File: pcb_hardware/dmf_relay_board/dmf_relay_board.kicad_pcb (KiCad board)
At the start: 2 copper layers, 100 x 96.5 mm, 64 parts, among them J1 HVPS, J2 Relays to Electrodes 1, J3 Relays to Electrodes 2, J4 Electrodes from Relay 1, J5 Electrodes from Relay 2, U1 HV507

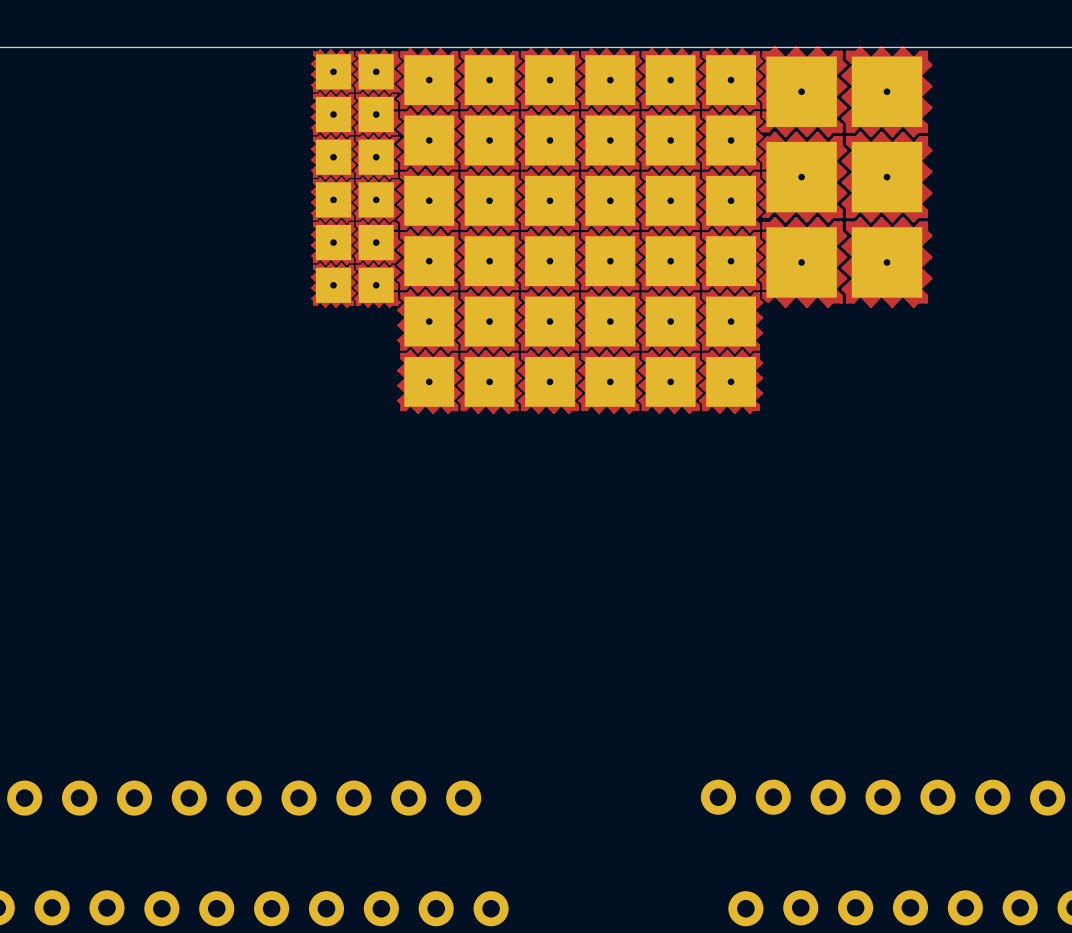
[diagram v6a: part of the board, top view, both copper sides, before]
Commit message: electrode footprints placed - routing now
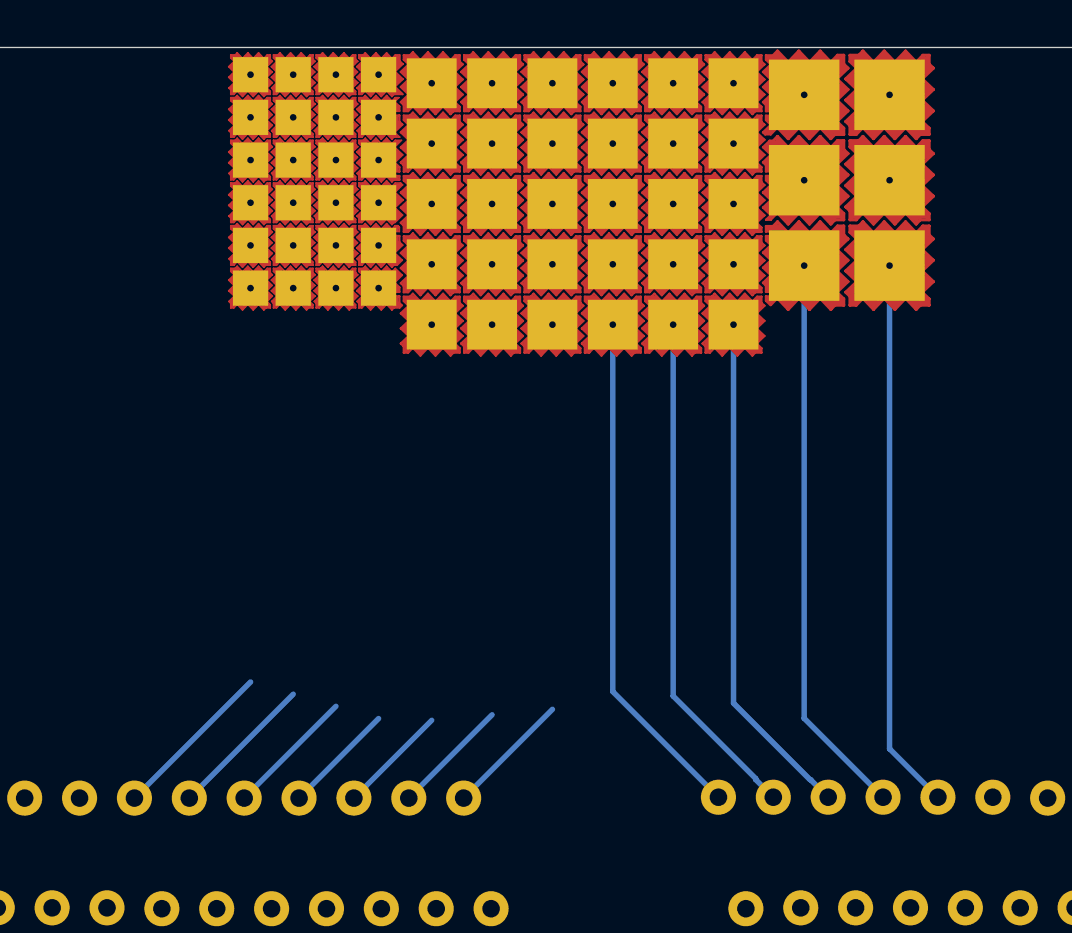
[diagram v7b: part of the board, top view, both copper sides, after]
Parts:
- removed E1, E10, E11, E12, E13, E14, E15, E16, E17, E18, E19, E2, E20, E21, E22, E23, E24, E25, E26, E27, E28, E29, E3, E30, E31, E32, E33, E34, E35, E36, E4, E5, E6, E7, E8, E9: ELEC_SML, dmf_relay_board:ELECTRODE_2_75_4MIL_4_5
- removed E50, E51, E52, E53, E54, E55: ELEC_XS, dmf_relay_board:ELECTRODE_1_375_4MIL_4_5
- removed the REF** at (174.5, 63.8)
- removed the REF** at (151.2, 61.0)
- removed the REF** at (151.2, 59.0)
- removed the REF** at (151.2, 57.1)
- removed the REF** at (151.2, 55.2)
- removed the REF** at (174.5, 59.9)
- removed the REF** at (174.5, 56.1)
- removed the REF** at (170.6, 63.8)
- removed the REF** at (170.6, 59.9)
- removed the REF** at (170.6, 56.1)
- removed the REF** at (151.2, 64.9)
- removed the REF** at (151.2, 62.9)
- added ELG1: ELEC_SM_TO_LG_1, dmf_relay_board:ELEC_SM_TO_LG_NUM1, F.Cu at (170.7, 56.2)
- added ELG2: ELEC_LG, dmf_relay_board:ELECTRODE_3_89_4MIL_4_5, F.Cu at (174.6, 56.2)
- added ELG3: ELEC_SM_TO_LG_2, dmf_relay_board:ELEC_SM_TO_LG_NUM2, F.Cu at (170.7, 60.1)
- added ELG4: ELEC_LG, dmf_relay_board:ELECTRODE_3_89_4MIL_4_5, F.Cu at (174.6, 60.1)
- added ELG5: ELEC_SM_TO_LG_3, dmf_relay_board:ELEC_SM_TO_LG_NUM3, F.Cu at (170.7, 64.0)
- added ELG6: ELEC_LG, dmf_relay_board:ELECTRODE_3_89_4MIL_4_5, F.Cu at (174.6, 64.0)
- added ESM1: ELEC_SML, dmf_relay_board:ELECTRODE_2_75_4MIL_4_5, F.Cu at (153.7, 55.7)
- added ESM10: ELEC_SML, dmf_relay_board:ELECTRODE_2_75_4MIL_4_5, F.Cu at (162.0, 58.4)
- added ESM11: ELEC_SML, dmf_relay_board:ELECTRODE_2_75_4MIL_4_5, F.Cu at (164.7, 58.4)
- added ESM12: ELEC_SML, dmf_relay_board:ELECTRODE_2_75_4MIL_4_5, F.Cu at (167.5, 58.4)
- added ESM13: ELEC_SML, dmf_relay_board:ELECTRODE_2_75_4MIL_4_5, F.Cu at (153.7, 61.2)
- added ESM14: ELEC_SML, dmf_relay_board:ELECTRODE_2_75_4MIL_4_5, F.Cu at (156.5, 61.2)
- added ESM15: ELEC_SML, dmf_relay_board:ELECTRODE_2_75_4MIL_4_5, F.Cu at (159.2, 61.2)
- added ESM16: ELEC_SML, dmf_relay_board:ELECTRODE_2_75_4MIL_4_5, F.Cu at (162.0, 61.2)
- added ESM17: ELEC_SML, dmf_relay_board:ELECTRODE_2_75_4MIL_4_5, F.Cu at (164.7, 61.2)
- added ESM18: ELEC_SML, dmf_relay_board:ELECTRODE_2_75_4MIL_4_5, F.Cu at (167.5, 61.2)
- added ESM19: ELEC_SML, dmf_relay_board:ELECTRODE_2_75_4MIL_4_5, F.Cu at (153.7, 63.9)
- added ESM2: ELEC_SML, dmf_relay_board:ELECTRODE_2_75_4MIL_4_5, F.Cu at (156.5, 55.7)
- added ESM20: ELEC_SML, dmf_relay_board:ELECTRODE_2_75_4MIL_4_5, F.Cu at (156.5, 63.9)
- added ESM21: ELEC_SML, dmf_relay_board:ELECTRODE_2_75_4MIL_4_5, F.Cu at (159.2, 63.9)
- added ESM22: ELEC_SML, dmf_relay_board:ELECTRODE_2_75_4MIL_4_5, F.Cu at (162.0, 63.9)
- added ESM23: ELEC_SML, dmf_relay_board:ELECTRODE_2_75_4MIL_4_5, F.Cu at (164.7, 63.9)
- added ESM24: ELEC_SML, dmf_relay_board:ELECTRODE_2_75_4MIL_4_5, F.Cu at (167.5, 63.9)
- added ESM25: ELEC_SML, dmf_relay_board:ELECTRODE_2_75_4MIL_4_5, F.Cu at (153.7, 66.7)
- added ESM26: ELEC_SML, dmf_relay_board:ELECTRODE_2_75_4MIL_4_5, F.Cu at (156.5, 66.7)
- added ESM27: ELEC_SML, dmf_relay_board:ELECTRODE_2_75_4MIL_4_5, F.Cu at (159.2, 66.7)
- added ESM28: ELEC_SML, dmf_relay_board:ELECTRODE_2_75_4MIL_4_5, F.Cu at (162.0, 66.7)
- added ESM29: ELEC_SML, dmf_relay_board:ELECTRODE_2_75_4MIL_4_5, F.Cu at (164.7, 66.7)
- added ESM3: ELEC_SML, dmf_relay_board:ELECTRODE_2_75_4MIL_4_5, F.Cu at (159.2, 55.7)
- added ESM30: ELEC_SML, dmf_relay_board:ELECTRODE_2_75_4MIL_4_5, F.Cu at (167.5, 66.7)
- added ESM4: ELEC_SML, dmf_relay_board:ELECTRODE_2_75_4MIL_4_5, F.Cu at (162.0, 55.7)
- added ESM5: ELEC_SML, dmf_relay_board:ELECTRODE_2_75_4MIL_4_5, F.Cu at (164.7, 55.7)
- added ESM6: ELEC_SML, dmf_relay_board:ELECTRODE_2_75_4MIL_4_5, F.Cu at (167.5, 55.7)
- added ESM7: ELEC_SML, dmf_relay_board:ELECTRODE_2_75_4MIL_4_5, F.Cu at (153.7, 58.4)
- added ESM8: ELEC_SML, dmf_relay_board:ELECTRODE_2_75_4MIL_4_5, F.Cu at (156.5, 58.4)
- added ESM9: ELEC_SML, dmf_relay_board:ELECTRODE_2_75_4MIL_4_5, F.Cu at (159.2, 58.4)
- added EXS1: ELEC_XS, dmf_relay_board:ELECTRODE_1_375_4MIL_4_5, F.Cu at (145.5, 55.3)
- added EXS10: ELEC_XS, dmf_relay_board:ELECTRODE_1_375_4MIL_4_5, F.Cu at (147.4, 59.2)
- added EXS11: ELEC_XS, dmf_relay_board:ELECTRODE_1_375_4MIL_4_5, F.Cu at (149.4, 59.2)
- added EXS12: ELEC_XS_TO_SM_3, dmf_relay_board:ELEC_XS_TO_SM_NUM3, F.Cu at (151.3, 59.2)
- added EXS13: ELEC_XS, dmf_relay_board:ELECTRODE_1_375_4MIL_4_5, F.Cu at (145.5, 61.1)
- added EXS14: ELEC_XS, dmf_relay_board:ELECTRODE_1_375_4MIL_4_5, F.Cu at (147.4, 61.1)
- added EXS15: ELEC_XS, dmf_relay_board:ELECTRODE_1_375_4MIL_4_5, F.Cu at (149.4, 61.1)
- added EXS16: ELEC_XS_TO_SM_4, dmf_relay_board:ELEC_XS_TO_SM_NUM4, F.Cu at (151.3, 61.1)
- added EXS17: ELEC_XS, dmf_relay_board:ELECTRODE_1_375_4MIL_4_5, F.Cu at (145.5, 63.1)
- added EXS18: ELEC_XS, dmf_relay_board:ELECTRODE_1_375_4MIL_4_5, F.Cu at (147.4, 63.1)
- added EXS19: ELEC_XS, dmf_relay_board:ELECTRODE_1_375_4MIL_4_5, F.Cu at (149.4, 63.1)
- added EXS2: ELEC_XS, dmf_relay_board:ELECTRODE_1_375_4MIL_4_5, F.Cu at (147.4, 55.3)
- added EXS20: ELEC_XS_TO_SM_5, dmf_relay_board:ELEC_XS_TO_SM_NUM5, F.Cu at (151.3, 63.1)
- added EXS21: ELEC_XS, dmf_relay_board:ELECTRODE_1_375_4MIL_4_5, F.Cu at (145.5, 65.0)
- added EXS22: ELEC_XS, dmf_relay_board:ELECTRODE_1_375_4MIL_4_5, F.Cu at (147.4, 65.0)
- added EXS23: ELEC_XS, dmf_relay_board:ELECTRODE_1_375_4MIL_4_5, F.Cu at (149.4, 65.0)
- added EXS24: ELEC_XS_TO_SM_6, dmf_relay_board:ELEC_XS_TO_SM_NUM6, F.Cu at (151.3, 65.0)
- added EXS3: ELEC_XS, dmf_relay_board:ELECTRODE_1_375_4MIL_4_5, F.Cu at (149.4, 55.3)
- added EXS4: ELEC_XS_TO_SM_1, dmf_relay_board:ELEC_XS_TO_SM_NUM1, F.Cu at (151.3, 55.3)
- added EXS5: ELEC_XS, dmf_relay_board:ELECTRODE_1_375_4MIL_4_5, F.Cu at (145.5, 57.2)
- added EXS6: ELEC_XS, dmf_relay_board:ELECTRODE_1_375_4MIL_4_5, F.Cu at (147.4, 57.2)
- added EXS7: ELEC_XS, dmf_relay_board:ELECTRODE_1_375_4MIL_4_5, F.Cu at (149.4, 57.2)
- added EXS8: ELEC_XS_TO_SM_2, dmf_relay_board:ELEC_XS_TO_SM_NUM2, F.Cu at (151.3, 57.2)
- added EXS9: ELEC_XS, dmf_relay_board:ELECTRODE_1_375_4MIL_4_5, F.Cu at (145.5, 59.2)
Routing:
- net Net-(ELG5-Pad1): track 0.00 -> 25.7 mm
- net Net-(ELG6-Pad1): track 0.00 -> 25.1 mm
- net Net-(ESM28-Pad1): track 0.00 -> 23.5 mm
- net Net-(ESM29-Pad1): track 0.00 -> 23.4 mm
- net Net-(ESM30-Pad1): track 0.00 -> 23.3 mm
- net Net-(EXS21-Pad1): track 0.00 -> 7.48 mm
- net Net-(EXS22-Pad1): track 0.00 -> 6.70 mm
- net Net-(EXS23-Pad1): track 0.00 -> 5.91 mm
- net Net-(ESM27-Pad1): track 0.00 -> 5.72 mm
- net Net-(ESM26-Pad1): track 0.00 -> 5.37 mm
- net Net-(EXS24-Pad1): track 0.00 -> 5.13 mm
- net Net-(ESM25-Pad1): track 0.00 -> 5.01 mm

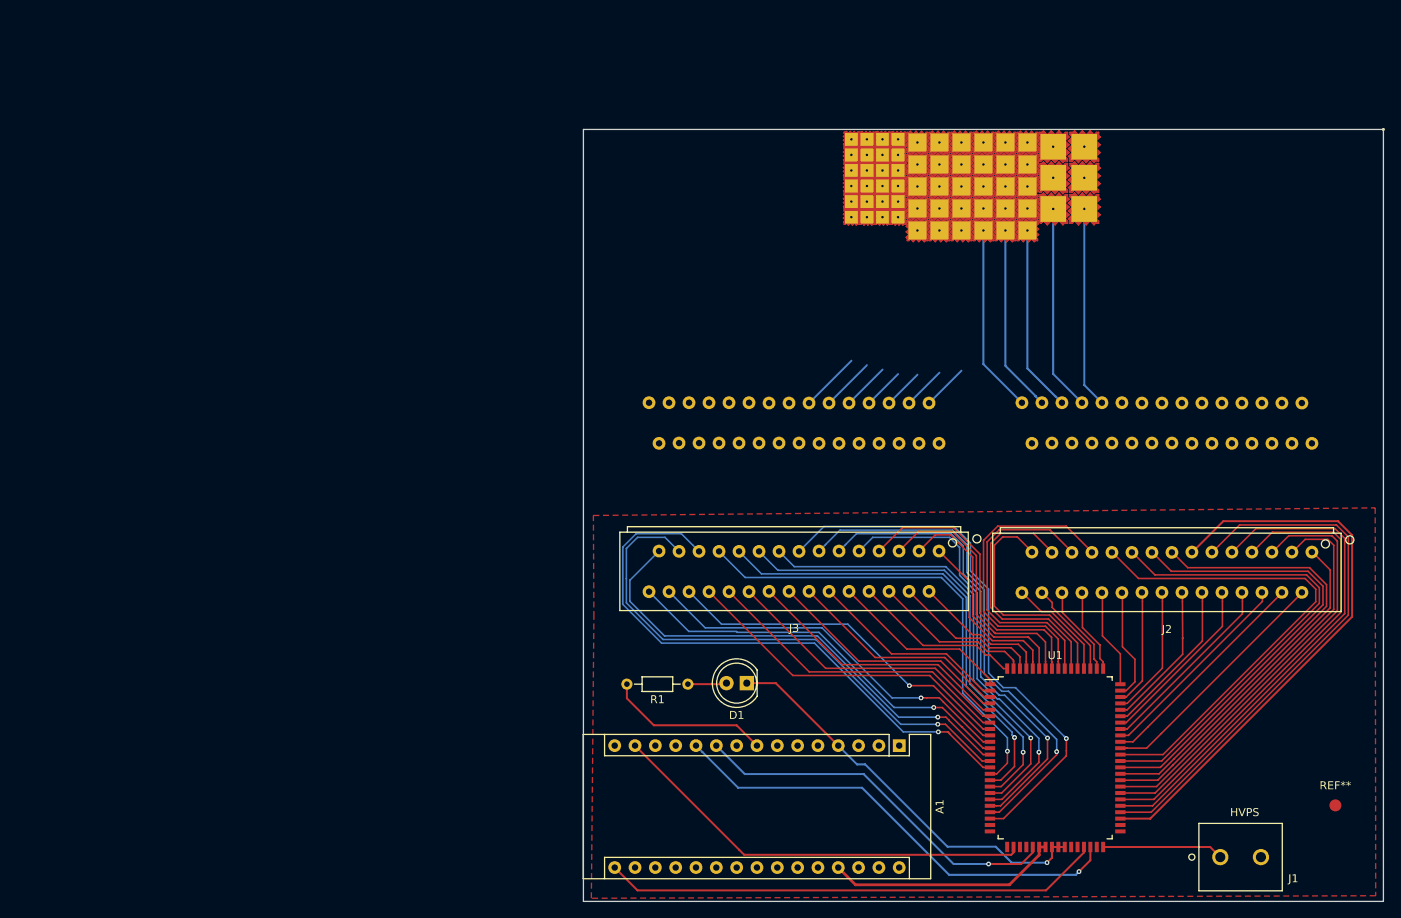
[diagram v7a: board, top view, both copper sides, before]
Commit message: electrode pads fixed for routing
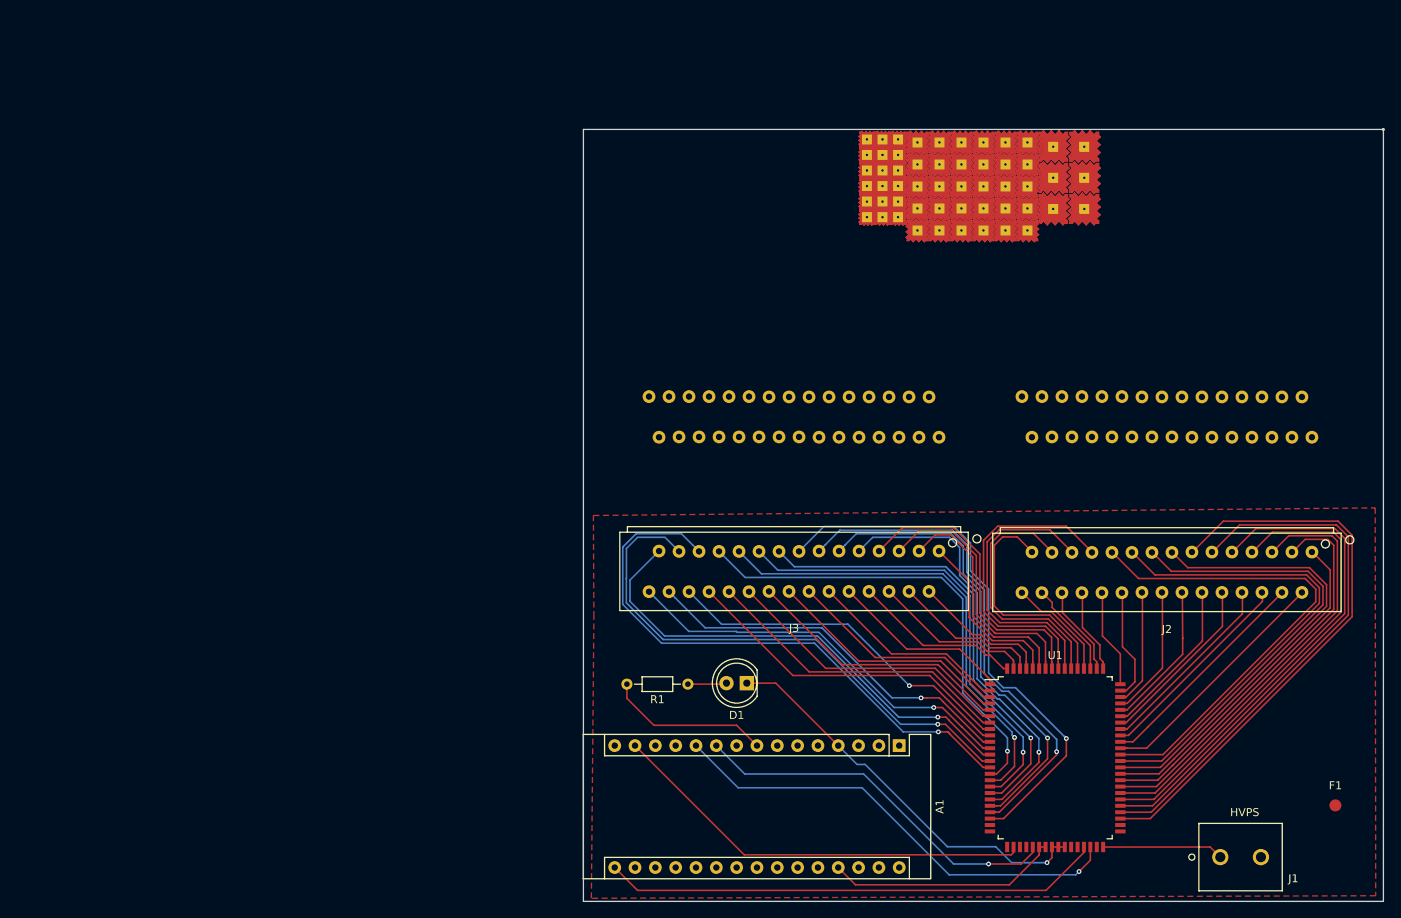
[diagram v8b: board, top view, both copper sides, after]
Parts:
- removed EXS19, EXS21, EXS22, EXS23: ELEC_XS, dmf_relay_board:ELECTRODE_1_375_4MIL_4_5
- removed EXS20: ELEC_XS_TO_SM_5, dmf_relay_board:ELEC_XS_TO_SM_NUM5
- removed EXS24: ELEC_XS_TO_SM_6, dmf_relay_board:ELEC_XS_TO_SM_NUM6
- EXS12: value ELEC_XS_TO_SM_3 -> ELEC_XS_TO_SM_4; footprint dmf_relay_board:ELEC_XS_TO_SM_NUM3 -> dmf_relay_board:ELEC_XS_TO_SM_NUM4
- EXS15: value ELEC_XS -> ELEC_XS_TO_SM_5; footprint dmf_relay_board:ELECTRODE_1_375_4MIL_4_5 -> dmf_relay_board:ELEC_XS_TO_SM_NUM5
- EXS16: value ELEC_XS_TO_SM_4 -> ELEC_XS; footprint dmf_relay_board:ELEC_XS_TO_SM_NUM4 -> dmf_relay_board:ELECTRODE_1_375_4MIL_4_5
- EXS18: value ELEC_XS -> ELEC_XS_TO_SM_6; footprint dmf_relay_board:ELECTRODE_1_375_4MIL_4_5 -> dmf_relay_board:ELEC_XS_TO_SM_NUM6
- EXS3: value ELEC_XS -> ELEC_XS_TO_SM_1; footprint dmf_relay_board:ELECTRODE_1_375_4MIL_4_5 -> dmf_relay_board:ELEC_XS_TO_SM_NUM1
- EXS4: value ELEC_XS_TO_SM_1 -> ELEC_XS; footprint dmf_relay_board:ELEC_XS_TO_SM_NUM1 -> dmf_relay_board:ELECTRODE_1_375_4MIL_4_5
- EXS6: value ELEC_XS -> ELEC_XS_TO_SM_2; footprint dmf_relay_board:ELECTRODE_1_375_4MIL_4_5 -> dmf_relay_board:ELEC_XS_TO_SM_NUM2
- EXS8: value ELEC_XS_TO_SM_2 -> ELEC_XS; footprint dmf_relay_board:ELEC_XS_TO_SM_NUM2 -> dmf_relay_board:ELECTRODE_1_375_4MIL_4_5
- EXS9: value ELEC_XS -> ELEC_XS_TO_SM_3; footprint dmf_relay_board:ELECTRODE_1_375_4MIL_4_5 -> dmf_relay_board:ELEC_XS_TO_SM_NUM3
- moved EXS9 5.84 mm to (151.3, 59.2)
- moved EXS16 5.50 mm to (147.4, 65.0)
- moved EXS17 4.35 mm to (149.4, 65.0)
- moved EXS18 4.35 mm to (151.3, 65.0)
- moved EXS4 4.35 mm to (147.4, 57.2)
- moved EXS5 3.89 mm to (149.4, 57.2)
- moved EXS6 3.89 mm to (151.3, 57.2)
- moved EXS13 2.75 mm to (147.4, 63.1)
- moved EXS14 2.75 mm to (149.4, 63.1)
- moved EXS15 2.75 mm to (151.3, 63.1)
- moved EXS7 2.75 mm to (147.4, 59.2)
- moved EXS8 2.75 mm to (149.4, 59.2)
- moved EXS10 1.95 mm to (147.4, 61.1)
- moved EXS11 1.95 mm to (149.4, 61.1)
- moved EXS12 1.95 mm to (151.3, 61.1)
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- renumbered REF** to F1
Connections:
- J4 pad 1: Net-(J4-Pad1) -> Net-(EXS1-Pad1)
- J4 pad 10: Net-(J4-Pad10) -> Net-(EXS8-Pad1)
- J4 pad 11: Net-(J4-Pad11) -> Net-(EXS9-Pad1)
- J4 pad 13: Net-(J4-Pad13) -> Net-(EXS10-Pad1)
- J4 pad 14: Net-(J4-Pad14) -> Net-(EXS11-Pad1)
- J4 pad 15: Net-(J4-Pad15) -> Net-(EXS12-Pad1)
- J4 pad 17: Net-(J4-Pad17) -> Net-(EXS13-Pad1)
- J4 pad 18: Net-(J4-Pad18) -> Net-(EXS14-Pad1)
- J4 pad 19: Net-(J4-Pad19) -> Net-(EXS15-Pad1)
- J4 pad 2: Net-(J4-Pad2) -> Net-(EXS2-Pad1)
- J4 pad 3: Net-(J4-Pad3) -> Net-(EXS3-Pad1)
- J4 pad 5: Net-(J4-Pad5) -> Net-(EXS4-Pad1)
- J4 pad 6: Net-(J4-Pad6) -> Net-(EXS5-Pad1)
- J4 pad 7: Net-(J4-Pad7) -> Net-(EXS6-Pad1)
- J4 pad 9: Net-(J4-Pad9) -> Net-(EXS7-Pad1)
- J5 pad 12: Net-(EXS22-Pad1) -> Net-(EXS17-Pad1)
- J5 pad 14: Net-(EXS21-Pad1) -> Net-(EXS16-Pad1)
- J5 pad 18: Net-(EXS14-Pad1) -> Net-(J5-Pad18)
- J5 pad 2: Net-(ESM27-Pad1) -> Net-(J5-Pad2)
- J5 pad 4: Net-(ESM26-Pad1) -> Net-(J5-Pad4)
- J5 pad 6: Net-(ESM25-Pad1) -> Net-(J5-Pad6)
- J5 pad 8: Net-(EXS24-Pad1) -> Net-(EXS18-Pad1)
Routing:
- net Net-(ELG5-Pad1): track 25.7 -> 0.00 mm
- net Net-(ELG6-Pad1): track 25.1 -> 0.00 mm
- net Net-(ESM28-Pad1): track 23.5 -> 0.00 mm
- net Net-(ESM29-Pad1): track 23.4 -> 0.00 mm
- net Net-(ESM30-Pad1): track 23.3 -> 0.00 mm
- net Net-(EXS21-Pad1): track 7.48 -> 0.00 mm
- net Net-(EXS22-Pad1): track 6.70 -> 0.00 mm
- net Net-(J5-Pad10): track 5.91 -> 0.00 mm
- net Net-(ESM27-Pad1): track 5.72 -> 0.00 mm
- net Net-(ESM26-Pad1): track 5.37 -> 0.00 mm
- net Net-(EXS24-Pad1): track 5.13 -> 0.00 mm
- net Net-(ESM25-Pad1): track 5.01 -> 0.00 mm
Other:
- net class ELEC_HV added: clearance 0, trace_width 0.2, via_dia 0.6, via_drill 0.3
